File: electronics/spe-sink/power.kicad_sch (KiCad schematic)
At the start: 27 parts, among them P2 CONN_01X02, U5 AP2112K-3.3, U6 INA180A3, U7 TLVM23625RDNR, U8 TPS26625

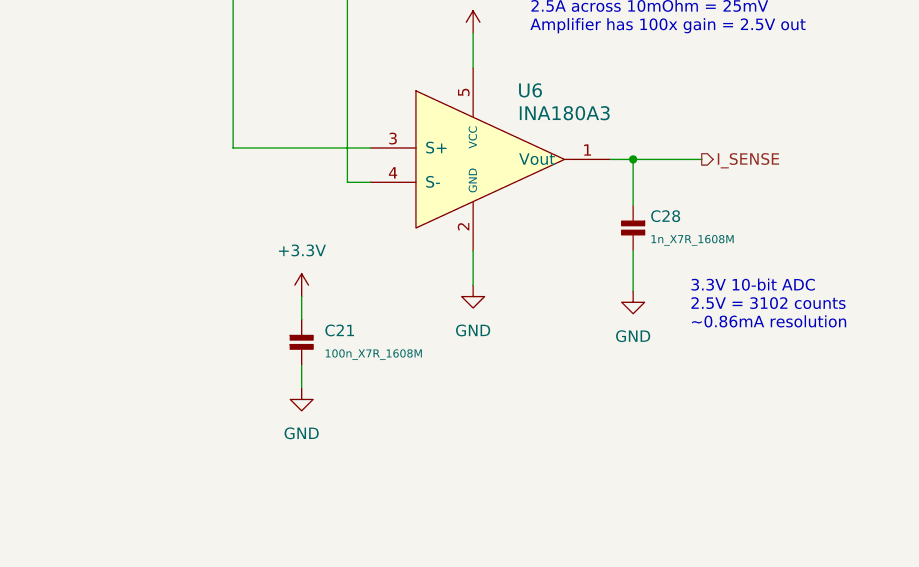
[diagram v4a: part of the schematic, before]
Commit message: PD sink PCB design 'finished', page cleanup, etc
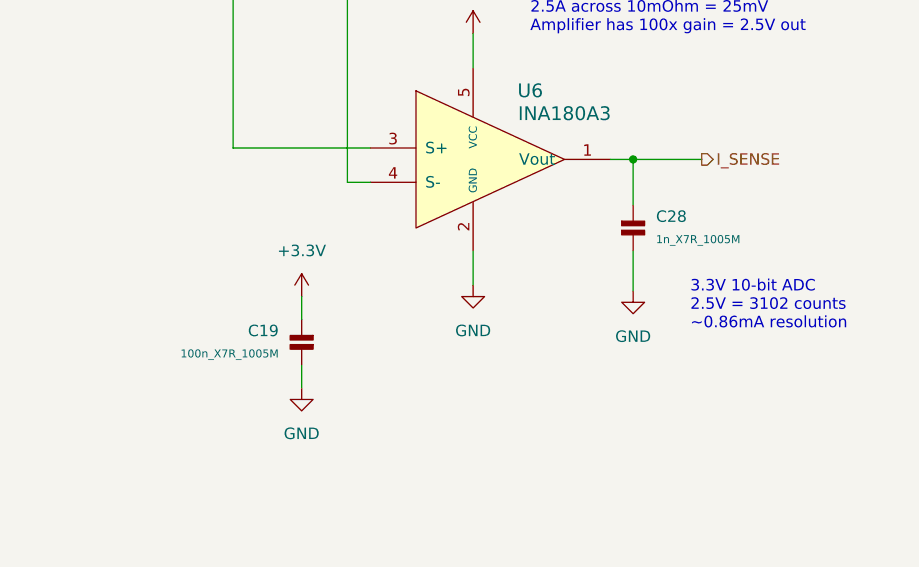
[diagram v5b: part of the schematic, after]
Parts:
- removed C21: 100n_X7R_1608M, Applidyne_Capacitor:CAPC1608X90N, symbol appli_capacitor:100n_X7R_1608M
- removed C28: 1n_X7R_1608M, Applidyne_Capacitor:CAPC1608X90N, symbol appli_capacitor:1n_X7R_1608M
- added C19: 100n_X7R_1005M, Applidyne_Capacitor:CAPC1005X60N, symbol appli_capacitor:100n_X7R_1005M
- added C28: 1n_X7R_1005M, Applidyne_Capacitor:CAPC1005X60N, symbol appli_capacitor:1n_X7R_1005M
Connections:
- net +3.3V: now also C19.1
- net GND: now also C19.2, C28.2
- net I_SENSE: now also C28.1
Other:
- title: (none) -> PoDL Handling and Regulation
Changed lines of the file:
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@@
 (kicad_sch (version 20230121) (generator eeschema)
   (paper "A4")
+  (title_block
+    (title "PoDL Handling and Regulation")
+    (date "2023-08-16")
+    (rev "V1.0")
+    (comment 1 "also back-feeds MicroMod carrier board")
+    (comment 2 "Regulator provides bulk 5V which powers local 3.3")
+    (comment 3 "Input switch only activates after PSE starts")
+  )
   (junction (at 123.19 38.1) (diameter 0) (color 0 0 0 0)
   )
@@
       (effects (font (size 1.524 1.524)) hide)
     )
-    (property "Datasheet" "https://au.mouser.com/datasheet/2/196/Infineon-DPS310-DataSheet-v01_01-EN-1226485.pdf" (at 61.595 81.534 0)
+    (property "Datasheet" "https://www.ti.com/general/docs/suppproductinfo.tsp?distId=10&gotoUrl=https%3A%2F%2Fwww.ti.com%2Flit%2Fgpn%2Ftps2662" (at 61.595 81.534 0)
       (effects (font (size 1.524 1.524)) hide)
     )
@@
     )
   )
+  (symbol (lib_id "appli_capacitor:100n_X7R_1005M") (at 218.44 119.38 0) (mirror y) (unit 1)
+    (in_bom yes) (on_board yes) (dnp no)
+    (property "Reference" "C19" (at 215.9 120.65 0)
+      (effects (font (size 1.27 1.27)) (justify left))
+    )
+    (property "Value" "100n_X7R_1005M" (at 215.9 123.19 0)
+      (effects (font (size 0.889 0.889)) (justify left))
+    )
+    (property "Footprint" "Applidyne_Capacitor:CAPC1005X60N" (at 215.519 121.92 90)
+      (effects (font (size 0.508 0.508)) hide)
+    )
+    (property "Datasheet" "http://www.farnell.com/datasheets/1936565.pdf" (at 214.884 121.92 90)
+      (effects (font (size 0.508 0.508)) hide)
+    )
+    (property "manf" "TDK" (at 213.614 121.92 90)
+      (effects (font (size 0.508 0.508)) hide)
+    )
+    (property "manf#" "CGA2B3X7R1H104K050BB" (at 212.979 121.92 90)
+      (effects (font (size 0.508 0.508)) hide)
+    )
+    (property "Supplier" "Element14" (at 212.344 121.92 90)
+      (effects (font (size 0.508 0.508)) hide)
+    )
+    (property "Supplier Part No" "2210822" (at 211.709 121.92 90)
+      (effects (font (size 0.508 0.508)) hide)
+    )
+    (property "Supplier URL" "http://au.element14.com/tdk/cga2b3x7r1h104k050bb/cap-mlcc-x7r-100nf-50v-0402/dp/2210822" (at 211.074 121.92 90)
+      (effects (font (size 0.508 0.508)) hide)
+    )
+    (property "Supplier Price" "0.087" (at 210.439 121.92 90)
+      (effects (font (size 0.508 0.508)) hide)
+    )
+    (property "Supplier Price Break" "100" (at 209.804 121.92 90)
+      (effects (font (size 0.508 0.508)) hide)
+    )
+    (pin "1")
+    (pin "2")
+    (instances
+      (project "spe-sink"
+        (path "/f0a501c7-1ad1-4c59-9255-3d6aa4545d8b/d2c298ab-d4a2-4c33-86fb-9b17f2cedd7c"
+          (reference "C19") (unit 1)
+        )
+      )
+    )
+  )
   (symbol (lib_id "appli_power:GND") (at 99.06 71.12 0) (unit 1)
     (in_bom yes) (on_board yes) (dnp no) (fields_autoplaced)
@@
         (path "/f0a501c7-1ad1-4c59-9255-3d6aa4545d8b/d2c298ab-d4a2-4c33-86fb-9b17f2cedd7c"
           (reference "C31") (unit 1)
-        )
-      )
-    )
-  )
-  (symbol (lib_id "appli_capacitor:1n_X7R_1608M") (at 255.27 106.68 0) (mirror y) (unit 1)
-    (in_bom yes) (on_board yes) (dnp no) (fields_autoplaced)
-    (property "Reference" "C28" (at 257.175 107.95 0)
-      (effects (font (size 1.27 1.27)) (justify right))
-    )
-    (property "Value" "1n_X7R_1608M" (at 257.175 110.49 0)
-      (effects (font (size 0.889 0.889)) (justify right))
-    )
-    (property "Footprint" "Applidyne_Capacitor:CAPC1608X90N" (at 252.349 109.22 90)
-      (effects (font (size 0.508 0.508)) hide)
-    )
-    (property "Datasheet" "http://www.farnell.com/datasheets/1679506.pdf" (at 251.714 109.22 90)
-      (effects (font (size 0.508 0.508)) hide)
-    )
-    (property "manf" "AVX" (at 250.444 109.22 90)
-      (effects (font (size 0.508 0.508)) hide)
-    )
-    (property "manf#" "06031C102KAT2A" (at 249.809 109.22 90)
-      (effects (font (size 0.508 0.508)) hide)
-    )
-    (property "Supplier" "Element14" (at 249.174 109.22 90)
-      (effects (font (size 0.508 0.508)) hide)
-    )
-    (property "Supplier Part No" "1833874" (at 248.539 109.22 90)
-      (effects (font (size 0.508 0.508)) hide)
-    )
-    (property "Supplier URL" "http://au.element14.com/avx/06031c102kat2a/cap-mlcc-x7r-1nf-100v-0603/dp/1833874?ost=1833874" (at 247.904 109.22 90)
-      (effects (font (size 0.508 0.508)) hide)
-    )
-    (property "Supplier Price" "0.004" (at 247.269 109.22 90)
-      (effects (font (size 0.508 0.508)) hide)
-    )
-    (property "Supplier Price Break" "10" (at 246.634 109.22 90)
-      (effects (font (size 0.508 0.508)) hide)
-    )
-    (pin "1")
-    (pin "2")
-    (instances
-      (project "spe-sink"
-        (path "/f0a501c7-1ad1-4c59-9255-3d6aa4545d8b/d2c298ab-d4a2-4c33-86fb-9b17f2cedd7c"
-          (reference "C28") (unit 1)
         )
       )
@@
     )
   )
-  (symbol (lib_id "appli_capacitor:100n_X7R_1608M") (at 218.44 119.38 0) (unit 1)
-    (in_bom yes) (on_board yes) (dnp no) (fields_autoplaced)
-    (property "Reference" "C21" (at 220.98 120.65 0)
-      (effects (font (size 1.27 1.27)) (justify left))
-    )
-    (property "Value" "100n_X7R_1608M" (at 220.98 123.19 0)
-      (effects (font (size 0.889 0.889)) (justify left))
-    )
-    (property "Footprint" "Applidyne_Capacitor:CAPC1608X90N" (at 221.361 121.92 90)
-      (effects (font (size 0.508 0.508)) hide)
-    )
-    (property "Datasheet" "http://www.farnell.com/datasheets/1732728.pdf" (at 221.996 121.92 90)
-      (effects (font (size 0.508 0.508)) hide)
-    )
-    (property "manf" "KEMET" (at 223.266 121.92 90)
-      (effects (font (size 0.508 0.508)) hide)
-    )
-    (property "manf#" "C0603C104K5RACAUTO" (at 223.901 121.92 90)
-      (effects (font (size 0.508 0.508)) hide)
-    )
-    (property "Supplier" "Element14" (at 224.536 121.92 90)
-      (effects (font (size 0.508 0.508)) hide)
-    )
-    (property "Supplier Part No" "2070398" (at 225.171 121.92 90)
-      (effects (font (size 0.508 0.508)) hide)
-    )
-    (property "Supplier URL" "http://au.element14.com/kemet/c0603c104k5racauto/cap-mlcc-x7r-100nf-50v-0603/dp/2070398" (at 225.806 121.92 90)
-      (effects (font (size 0.508 0.508)) hide)
-    )
-    (property "Supplier Price" "0.011" (at 226.441 121.92 90)
-      (effects (font (size 0.508 0.508)) hide)
-    )
-    (property "Supplier Price Break" "1" (at 227.076 121.92 90)
-      (effects (font (size 0.508 0.508)) hide)
-    )
-    (pin "1")
-    (pin "2")
-    (instances
-      (project "spe-sink"
-        (path "/f0a501c7-1ad1-4c59-9255-3d6aa4545d8b"
-          (reference "C21") (unit 1)
-        )
-        (path "/f0a501c7-1ad1-4c59-9255-3d6aa4545d8b/d2c298ab-d4a2-4c33-86fb-9b17f2cedd7c"
-          (reference "C19") (unit 1)
-        )
-      )
-    )
-  )
   (symbol (lib_id "appli_resistor:40K2_1005M") (at 162.56 43.18 0) (unit 1)
     (in_bom yes) (on_board yes) (dnp no) (fields_autoplaced)
@@
         )
       )
+    )
+  )
+  (symbol (lib_id "appli_capacitor:1n_X7R_1005M") (at 255.27 106.68 0) (unit 1)
+    (in_bom yes) (on_board yes) (dnp no) (fields_autoplaced)
+    (property "Reference" "C28" (at 257.81 107.95 0)
+      (effects (font (size 1.27 1.27)) (justify left))
+    )
+    (property "Value" "1n_X7R_1005M" (at 257.81 110.49 0)
+      (effects (font (size 0.889 0.889)) (justify left))
+    )
+    (property "Footprint" "Applidyne_Capacitor:CAPC1005X60N" (at 258.191 109.22 90)
+      (effects (font (size 0.508 0.508)) hide)
+    )
+    (property "Datasheet" "http://www.farnell.com/datasheets/2205255.pdf" (at 258.826 109.22 90)
+      (effects (font (size 0.508 0.508)) hide)
+    )
+    (property "manf" "KEMET" (at 260.096 109.22 90)
+      (effects (font (size 0.508 0.508)) hide)
+    )
+    (property "manf#" "C0402C102K5RACTU" (at 260.731 109.22 90)
+      (effects (font (size 0.508 0.508)) hide)
+    )
+    (property "Supplier" "Element14" (at 261.366 109.22 90)
+      (effects (font (size 0.508 0.508)) hide)
+    )
+    (property "Supplier Part No" "1414573" (at 262.001 109.22 90)
+      (effects (font (size 0.508 0.508)) hide)
+    )
+    (property "Supplier URL" "http://au.element14.com/kemet/c0402c102k5ractu/cap-mlcc-x7r-1nf-50v-0402/dp/1414573" (at 262.636 109.22 90)
+      (effects (font (size 0.508 0.508)) hide)
+    )
+    (property "Supplier Price" "0.015" (at 263.271 109.22 90)
+      (effects (font (size 0.508 0.508)) hide)
+    )
+    (property "Supplier Price Break" "100" (at 263.906 109.22 90)
+      (effects (font (size 0.508 0.508)) hide)
+    )
+    (pin "1")
+    (pin "2")
+    (instances
+      (project "spe-sink"
+        (path "/f0a501c7-1ad1-4c59-9255-3d6aa4545d8b/d2c298ab-d4a2-4c33-86fb-9b17f2cedd7c"
+          (reference "C28") (unit 1)
+        )
+      )

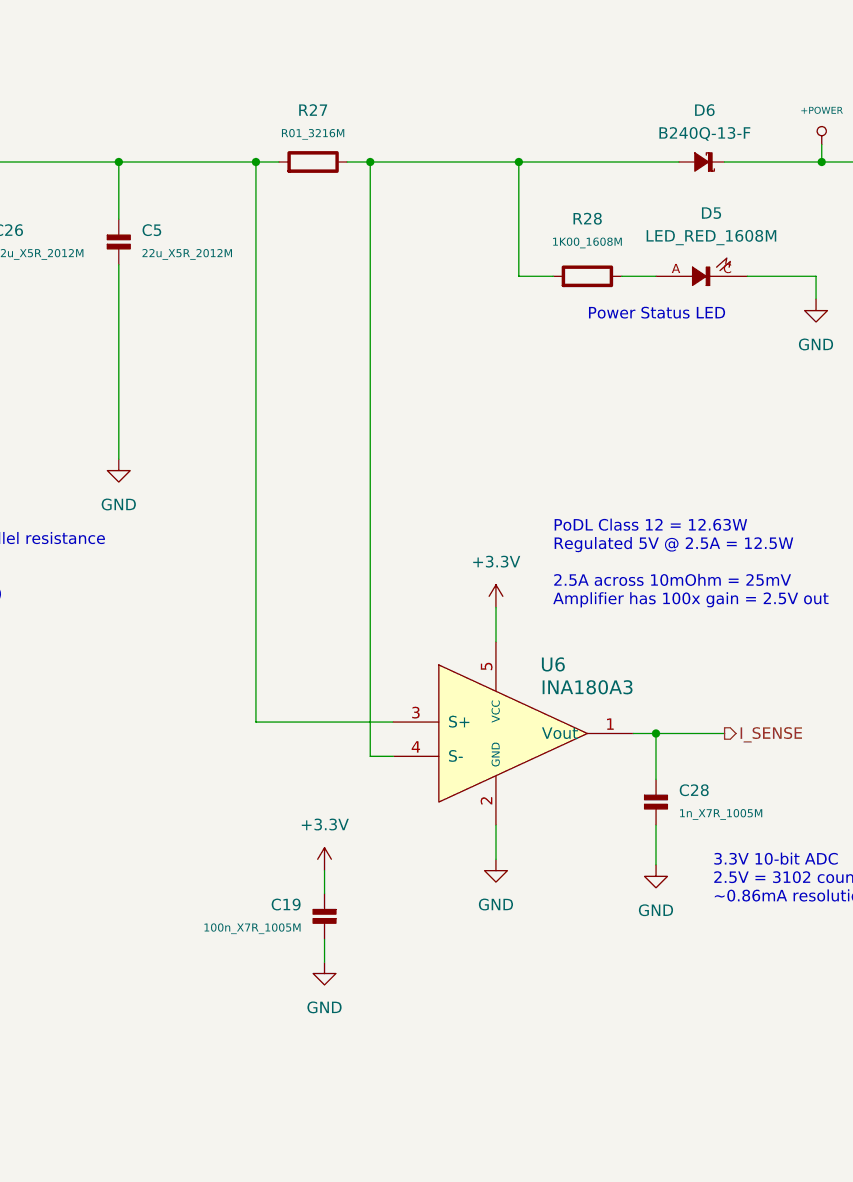
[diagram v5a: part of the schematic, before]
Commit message: Fix current amplifier part choice on PD board
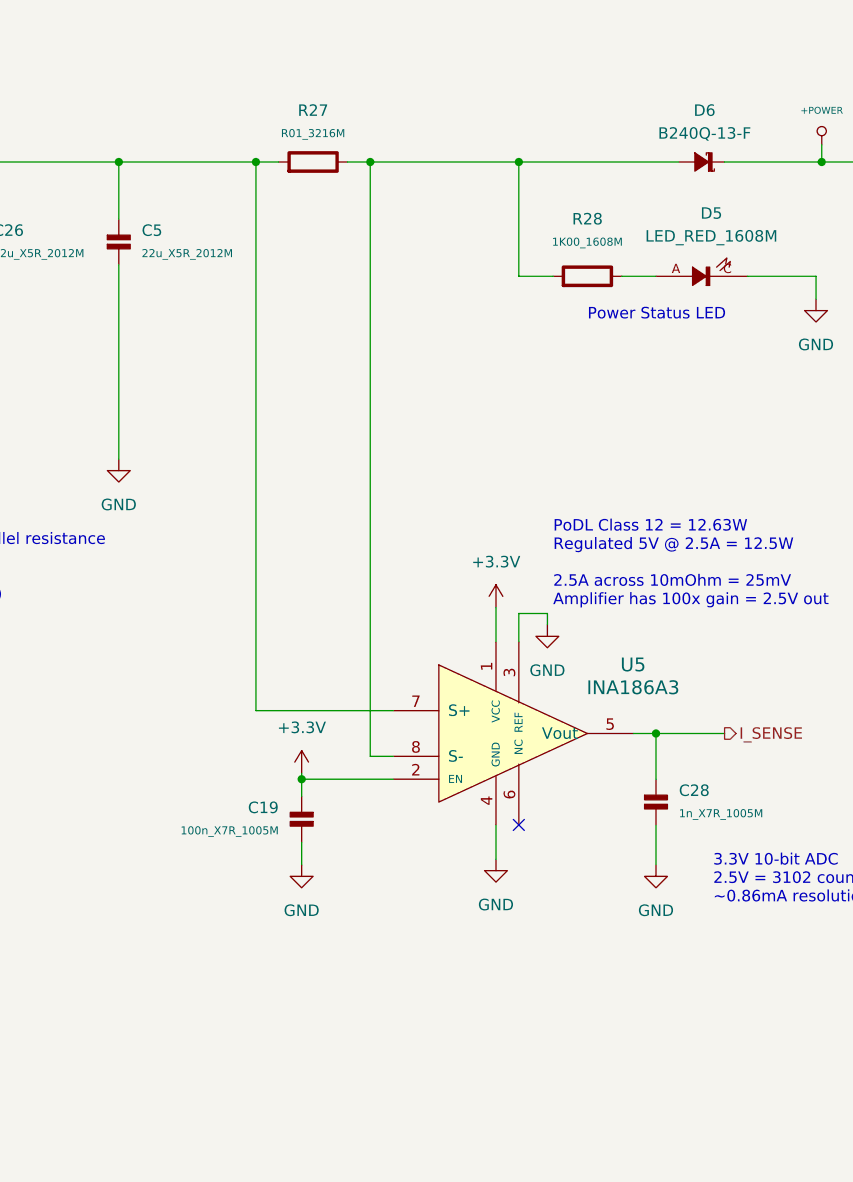
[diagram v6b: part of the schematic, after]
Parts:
- removed U6: INA180A3, Applidyne_SOT:SOT23-8P65_280X145L45X30N, symbol appli_analog_devices:INA180A3
- added U5: INA186A3, Applidyne_SOT:SOT23-8P65_280X145L45X30N, symbol appli_analog_devices:INA186A3
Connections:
- net +3.3V: now also U5.1 (VCC), U5.2 (EN)
- net GND: now also U5.3 (REF), U5.4 (GND)
- net I_SENSE: now also U5.5 (Vout)
- net at C26.1, C5.1, R27.1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: now also U5.7 (S+)
- net at D6.A, R27.2, R28.1: now also U5.8 (S-)
- no-connect marks 6 -> 7
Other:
- moved on the sheet: C19
